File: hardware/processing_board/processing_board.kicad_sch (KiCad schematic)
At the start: 43 parts, among them J1 USB_C_Receptacle_USB2.0_14P, J2 USB_C_Receptacle_USB2.0_14P, J3 S2B-PH-K-S_LF__SN_, U1 BQ24075RGT, U2 NCP1117-3.3_SOT223, U3 TPS62821DLC, U4 TPS22917DBV, U5 NCP1117-1.8_SOT223

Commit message: Added FPGA bypass caps
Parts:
- added C15: 3.3uF, symbol Device:C_Small_US
- added C16, C17: 18pF, symbol Device:C_Small_US
- added C18, C19, C20, C21, C22, C23, C24, C25, C26, C28: 0.1uF, symbol Device:C_Small_US
- added C27: 4.7uF, symbol Device:C_Small_US
- added C29: 100nF, symbol Device:C_Small_US
- added FB1: 600@100MHZ, symbol Device:FerriteBead_Small
- added IC1: XC7S25-2CSGA225I, BGA225C80P15X15_1300X1300X140, symbol XC7S25-2CSGA225I:XC7S25-2CSGA225I
- added J4: Micro_SD_Card_Det1, symbol Connector:Micro_SD_Card_Det1
- added R14: 12k, symbol Device:R_Small
- added R15, R24: 10k, symbol Device:R_Small
- added R16, R17: 1k, symbol Device:R_Small
- added R21: 2.2k, symbol Device:R_Small
- added R22: 330, symbol Device:R_Small
- added R23: 4.7k, symbol Device:R_Small
- added SW1: SW_Push, symbol Switch:SW_Push
- added TP4: GND_TP, TestPoint:TestPoint_Loop_D2.60mm_Drill0.9mm_Beaded, symbol Connector:TestPoint
- added U6: FT2232HQ, Package_DFN_QFN:QFN-64-1EP_9x9mm_P0.5mm_EP4.35x4.35mm, symbol Interface_USB:FT2232HQ
- added U7: 93LCxxA, symbol Memory_EEPROM:93LCxxA
- added U8: W25Q32JVSS, Package_SO:SOIC-8_5.3x5.3mm_P1.27mm, symbol Memory_Flash:W25Q32JVSS
- added X1: ESP32-S3-WROOM-1-N16R8, ESP32-S3-WROOM-1-N16R8:ESP32S3WROOM1N8R2, symbol ESP32-S3-WROOM-1-N16R8:ESP32-S3-WROOM-1-N16R8
- added Y1: Crystal, symbol Device:Crystal
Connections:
- net +1V0: now also IC1.E10 (VCCINT_2), IC1.E8 (VCCINT_1), IC1.F7 (VCCINT_3), IC1.G10 (VCCINT_4), IC1.G6 (VCCBRAM_1), IC1.H7 (VCCINT_5), IC1.J10 (VCCINT_6), IC1.J6 (VCCBRAM_2), IC1.K7 (VCCINT_7), IC1.K9 (VCCINT_8)
- net +1V8: now also FB1.1
- net +3V3: now also C18.1, C28.1, C29.1, IC1.B7 (VCCO_15_1), IC1.C11 (VCCO_15_2), IC1.C3 (VCCO_34_1), IC1.E6 (VCCO_0_1), IC1.G2 (VCCO_34_2), IC1.H5 (CFGBVS_0), IC1.J14 (VCCO_14_1), J4.4 (VDD), R15.1, R16.1, R22.1, R23.2, R24.1, U6.19 (ADBUS3), U6.50 (VREGIN), U7.8 (VCC), U8.8 (VCC), X1.2 (3V3)
- net FPGA_D+: now also U6.8 (DP)
- net FPGA_D-: now also U6.7 (DM)
- net GND: now also C15.2, C16.2, C17.2, C18.2, C19.2, C20.2, C21.2, C22.2, C23.2, C24.2, C25.2, C26.2, C27.2, C28.2, C29.2, IC1.A1 (GND_1), IC1.A15 (GND_2), IC1.B8 (GND_3), IC1.C12 (GND_5), IC1.C2 (GND_4), IC1.D14 (GND_7), IC1.D5 (VCCBATT_0), IC1.D6 (GND_6), IC1.E4 (GND_8), IC1.E7 (GND_9), IC1.E9 (GND_10), IC1.F10 (GND_12), IC1.F13 (GND_13), IC1.F6 (GND_11), IC1.F8 (GNDADC_0), IC1.G3 (GND_14), IC1.G8 (VREFN_0), IC1.G9 (VP_0), IC1.H10 (GND_17), IC1.H6 (GND_16), IC1.H8 (VN_0), IC1.H9 (VREFP_0), IC1.J13 (GND_19), IC1.J7 (GND_18), IC1.K10 (GND_22), IC1.K6 (GND_20), IC1.K8 (GND_21), IC1.L2 (GND_23), IC1.L7 (GND_24), IC1.L9 (GND_25), IC1.M11 (GND_26), IC1.P13 (GND_29), IC1.P4 (GND_27), IC1.P8 (GND_28), IC1.R1 (GND_30), IC1.R15 (GND_31), J4.10 (SHIELD), J4.6 (VSS), R14.1, R17.2, SW1.2, TP4.1, U6.1 (GND), U6.10 (AGND), U6.11 (GND), U6.15 (GND), U6.25 (GND), U6.35 (GND), U6.47 (GND), U6.5 (GND), U6.51 (GND), U6.65 (GND), U7.5 (GND), U8.4 (GND), X1.1 (GND), X1.40 (GND), X1.41 (GND), X1.42 (GND), X1.43 (GND), X1.44 (GND), X1.45 (GND), X1.46 (GND), X1.47 (GND), X1.48 (GND), X1.49 (GND)
- new net: C16.1, C17.1, U6.3 (OSCO), Y1.1
- new net: R15.2, U6.14 (~{RESET})
- new net: R21.1, U7.3 (DI)
- new net: R21.2, U6.61 (EEDATA), U7.4 (DO)
- new net: C26.1, C27.1, FB1.2, IC1.F9 (VCCADC_0)
- new net: IC1.G5 (DONE_0), R22.2
- new net: U6.2 (OSCI), Y1.2
- new net: R14.2, U6.6 (REF)
- new net: IC1.J5 (PROGRAM_B_0), R23.1, SW1.1
- new net BOOT: X1.27 (IO0)
- new net D+: X1.14 (IO20)
- new net D-: X1.13 (IO19)
- new net EECLK: U6.62 (EECLK), U7.2 (SCLK)
- new net EECS: U6.63 (EECS), U7.1 (CS)
- new net EN: X1.3 (EN)
- new net FLASH_CLK: IC1.F5 (CCLK_0), U8.6 (CLK)
- new net FLASH_CS: U8.1 (~{CS})
- new net FLASH_DI: IC1.H14 (IO_L1P_T0_D00_MOSI_14), U8.2 (DO/IO_{1})
- new net FLASH_DO: IC1.H15 (IO_L1N_T0_D01_DIN_14), U8.5 (DI/IO_{0})
- new net FLASH_HOLD: U8.7 (~{HOLD}/~{RESET}/IO_{3})
- new net FLASH_WP: IC1.J12 (IO_L2P_T0_D02_14), U8.3 (~{WP}/IO_{2})
- new net INT: X1.38 (IO2)
- new net IO11: X1.19 (IO11)
- new net IO12: X1.20 (IO12)
- new net IO13: X1.21 (IO13)
- new net IO14: X1.22 (IO14)
- new net IO4: X1.4 (IO4)
- new net IO5: X1.5 (IO5)
- new net IO6: X1.6 (IO6)
- new net IO7: X1.7 (IO7)
- new net IO8: X1.12 (IO8)
- new net RX: IC1.B5 (IO_L5N_T0_34)
- new net SD_CLK: J4.5 (CLK)
- new net SD_CMD: J4.3 (CMD)
- new net SD_DAT0: J4.7 (DAT0)
- new net SD_DAT3: J4.2 (DAT3/CD)
- new net SD_DET: J4.9 (DET), R24.2
- new net TCK: IC1.E5 (TCK_0), R17.1, U6.16 (ADBUS0)
- new net TDI: U6.17 (ADBUS1)
- new net TDO: IC1.K4 (TDO_0), U6.18 (ADBUS2)
- new net TMS: IC1.K5 (TMS_0), R16.2
- new net TX: IC1.C5 (IO_L5P_T0_34)
- new net VCCIO: C22.1, C23.1, C24.1, C25.1, U6.20 (VCCIO), U6.31 (VCCIO), U6.42 (VCCIO), U6.56 (VCCIO)
- new net VCORE: C19.1, C20.1, C21.1, U6.12 (VCORE), U6.37 (VCORE), U6.64 (VCORE)
- new net VPHY: U6.4 (VPHY)
- new net VPLL: U6.9 (VPLL)
- new net VREGOUT: C15.1, U6.49 (VREGOUT)
- no-connect marks 3 -> 58
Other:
- note added: "ESP32"
- moved on the sheet: C11, C12, C13, C14, C8, C9, R11, U4, U5

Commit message: Schematic is a disaster, passes ERC
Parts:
- removed J4: Micro_SD_Card_Det1, symbol Connector:Micro_SD_Card_Det1
- removed TP4: GND_TP, TestPoint:TestPoint_Loop_D2.60mm_Drill0.9mm_Beaded, symbol Connector:TestPoint
- removed U5: NCP1117-1.8_SOT223, Package_TO_SOT_SMD:SOT-223-3_TabPin2, symbol Regulator_Linear:NCP1117-1.8_SOT223
- added C30: 0.1uF, Capacitor_SMD:C_0805_2012Metric, symbol Device:C_Small_US
- added C31, C77, C78, C80: 0.1uF, symbol Device:C_Small_US
- added C32, C33, C41, C42, C47, C48, C55, C56, C60, C61, C71, C72, C73: 47nF, symbol Device:C_Small_US
- added C34, C35, C36, C37, C43, C44, C45, C46, C49, C50, C51, C52, C57, C62, C63, C66, C67, C74, C75: 470nF, symbol Device:C_Small_US
- added C38, C39, C53, C54, C59, C64, C68, C69: 4.7uF, symbol Device:C_Small_US
- added C40, C70: 100uF, symbol Device:C_Small_US
- added C58, C65: 47uF, symbol Device:C_Small_US
- added C76: 10nF, symbol Device:C_Small_US
- added C79, C81, C82: 0.01uF, symbol Device:C_Small_US
- added FB2: 600@100MHZ, symbol Device:FerriteBead_Small
- added FB3, FB4: 600@100MHz, symbol Device:FerriteBead_Small
- added J4: Conn_02x07_Counter_Clockwise, symbol Connector_Generic:Conn_02x07_Counter_Clockwise
- added LS1: Speaker, symbol Device:Speaker
- added R25, R26: 10k, Resistor_SMD:R_0805_2012Metric, symbol Device:R_Small
- added R27, R32: 4.7k, symbol Device:R_Small
- added R28, R29, R30, R31: 1k, symbol Device:R_Small
- added R33, R34, R35, R42: 10k, symbol Device:R_Small
- added R36, R37, R38, R39: 100, symbol Device:R_Small
- added R40, R41: 50, symbol Device:R_Small
- added SW2: BOOT_BTN, Button_Switch_SMD:SW_SPST_B3U-1000P, symbol Switch:SW_Push
- added SW3: RST_BTN, Button_Switch_SMD:SW_SPST_B3U-1000P, symbol Switch:SW_Push
- added U10: MAX98357A, Package_DFN_QFN:TQFN-16-1EP_3x3mm_P0.5mm_EP1.23x1.23mm, symbol Audio:MAX98357A
- added U11: LP2985-1.8, Package_TO_SOT_SMD:SOT-23-5, symbol Regulator_Linear:LP2985-1.8
- added U9: W25Q128JVS, Package_SO:SOIC-8_5.3x5.3mm_P1.27mm, symbol Memory_Flash:W25Q128JVS
- added Y2: ECS-2520MV-xxx-xx, Oscillator:Oscillator_SMD_ECS_2520MV-xxx-xx-4Pin_2.5x2.0mm, symbol Oscillator:ECS-2520MV-xxx-xx
- C2: value 10uF -> 22uF
- C26: value 0.1uF -> 47nF
- C27: value 4.7uF -> 470nF
- C29: value 100nF -> 0.1uF
- R22: value 330 -> 200
- R24: value 10k -> 100k
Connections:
- net 3V3_FPGA is gone; now on net +3.3V: C9.1, R13.1, U4.5 (QOD), U4.6 (VOUT)
- net D+ is gone; now on net ESP_D+: X1.14 (IO20)
- net D- is gone; now on net ESP_D-: X1.13 (IO19)
- net RX is gone; now on net ESP_TX: IC1.B5 (IO_L5N_T0_34)
- net TMS is gone; now on net +3.3V: IC1.K5 (TMS_0), R16.2
- net TX is gone; now on net ESP_RX: IC1.C5 (IO_L5P_T0_34)
- net +1V0: now also C55.1, C56.1, C57.1, C58.1, C59.1, C66.1, C67.1, C68.1, C69.1, C70.1, C71.1, C72.1, C73.1, C74.1
- net +1V8: now also IC1.D5 (VCCBATT_0), IC1.L6 (VCCAUX_1), IC1.L8 (VCCAUX_2), C60.1, C61.1, C62.1, C63.1, C64.1, C65.1, U11.5 (VOUT)
- net +3V3: now also C30.1, C77.1, R25.2, R26.2, R33.2, R34.2, R35.2, R42.1, U10.7 (VDD), U10.8 (VDD), U11.1 (VIN), U9.8 (VCC); no longer C28.1, IC1.B7 (VCCO_15_1), IC1.C11 (VCCO_15_2), IC1.C3 (VCCO_34_1), IC1.E6 (VCCO_0_1), IC1.G2 (VCCO_34_2), IC1.H5 (CFGBVS_0), IC1.J14 (VCCO_14_1), R16.1, R22.1, R23.2, U6.19 (ADBUS3), U8.8 (VCC)
- net 1V0_PG: now also R42.2, U11.3 (ON/~{OFF})
- net BOOT: now also R26.1, SW2.2
- net EN: now also R25.1, SW3.2
- net FLASH_CLK: now also R40.1; no longer IC1.F5 (CCLK_0)
- net FLASH_CS: now also IC1.L11 (IO_L6P_T0_FCS_B_14)
- net FLASH_DI: now also R36.2; no longer IC1.H14 (IO_L1P_T0_D00_MOSI_14)
- net FLASH_DO: now also R37.2; no longer IC1.H15 (IO_L1N_T0_D01_DIN_14)
- net FLASH_HOLD: now also R39.2
- net FLASH_WP: now also R38.2; no longer IC1.J12 (IO_L2P_T0_D02_14)
- net GND: now also IC1.G7 (GND_15), C30.2, C31.2, C32.2, C33.2, C34.2, C35.2, C36.2, C37.2, C38.2, C39.2, C40.2, C41.2, C42.2, C43.2, C44.2, C45.2, C46.2, C47.2, C48.2, C49.2, C50.2, C51.2, C52.2, C53.2, C54.2, C55.2, C56.2, C57.2, C58.2, C59.2, C60.2, C61.2, C62.2, C63.2, C64.2, C65.2, C66.2, C67.2, C68.2, C69.2, C70.2, C71.2, C72.2, C73.2, C74.2, C75.2, C77.2, C78.2, C79.2, C80.2, C81.2, C82.2, FB2.2, J4.8 (Pin_8), R30.2, R31.2, SW2.1, SW3.1, U10.11 (GND), U10.15 (GND), U10.17 (PAD), U10.3 (GND), U11.2 (GND), U9.4 (GND), Y2.2 (GND); no longer IC1.D5 (VCCBATT_0), IC1.F8 (GNDADC_0)
- net TDI: now also IC1.L4 (TDI_0)
- net VPHY: now also C78.1, C79.1, FB3.1
- net VPLL: now also C80.1, C81.1, FB4.1
- net ESP_TX: now reaches X1.17 (IO9)
- net ESP_CS: now reaches X1.18 (IO10)
- net ESP_CS: now also R35.1, U9.1 (~{CS})
- net +3.3V: now reaches C26.1, C27.1
- net +3.3V: now also C28.1, IC1.B7 (VCCO_15_1), IC1.C11 (VCCO_15_2), IC1.C3 (VCCO_34_1), IC1.E6 (VCCO_0_1), IC1.F12 (VCCO_15_3), IC1.G2 (VCCO_34_2), IC1.J14 (VCCO_14_1), IC1.L3 (VCCO_34_3), IC1.M12 (VCCO_14_2), IC1.P5 (VCCO_0_2), IC1.P9 (VCCO_14_3), R22.1, R23.2, U8.8 (VCC), C31.1, C32.1, C33.1, C34.1, C35.1, C36.1, C37.1, C38.1, C39.1, C40.1, C41.1, C42.1, C43.1, C44.1, C45.1, C46.1, C47.1, C48.1, C49.1, C50.1, C51.1, C52.1, C53.1, C54.1, FB3.2, FB4.2, J4.7 (Pin_7), R27.1, R28.1, R29.1, R32.1, Y2.1 (Tri-State), Y2.4 (VDD); no longer FB1.2, IC1.F9 (VCCADC_0)
- net BRIDGE_TX: now reaches U6.38 (BDBUS0)
- net BRIDGE_TX: now also IC1.K15 (IO_L5N_T0_D07_14)
- net BRIDGE_RX: now reaches U6.39 (BDBUS1)
- net BRIDGE_RX: now also IC1.L12 (IO_L6N_T0_D08_VREF_14)
- net FPGA_IO2: now reaches IC1.A3 (IO_L1N_T0_34)
- net FPGA_IO2: now also J4.2 (Pin_2)
- net FPGA_IO1: now reaches IC1.A4 (IO_L1P_T0_34)
- net FPGA_IO1: now also J4.1 (Pin_1)
- net FPGA_IO9: now reaches IC1.A5 (IO_L5P_T0_AD2P_15)
- net FPGA_IO9: now also J4.11 (Pin_11)
- net FPGA_IO10: now reaches IC1.A6 (IO_L5N_T0_AD2N_15)
- net FPGA_IO10: now also J4.12 (Pin_12)
- net FPGA_IO11: now reaches IC1.A8 (IO_L6P_T0_15)
- net FPGA_IO11: now also J4.13 (Pin_13)
- net FPGA_IO12: now reaches IC1.A9 (IO_L6N_T0_VREF_15)
- net FPGA_IO12: now also J4.14 (Pin_14)
- net FPGA_IO4: now reaches IC1.B3 (IO_L3N_T0_DQS_34)
- net FPGA_IO4: now also J4.4 (Pin_4)
- net FPGA_IO3: now reaches IC1.B4 (IO_L3P_T0_DQS_34)
- net FPGA_IO3: now also J4.3 (Pin_3)
- net FPGA_IO7: now reaches IC1.C6 (IO_L1P_T0_AD0P_15)
- net FPGA_IO7: now also J4.9 (Pin_9)
- net FPGA_IO8: now reaches IC1.C7 (IO_L1N_T0_AD0N_15)
- net FPGA_IO8: now also J4.10 (Pin_10)
- net FPGA_IO6: now reaches IC1.D1 (IO_L6N_T0_VREF_34)
- net FPGA_IO6: now also J4.6 (Pin_6)
- net FPGA_IO5: now reaches IC1.D2 (IO_L6P_T0_34)
- net FPGA_IO5: now also J4.5 (Pin_5)
- net at IC1.K11 (IO_L3P_T0_DQS_PUDC_B_14): now also R28.2
- net at IC1.K13 (IO_L2N_T0_D03_14): now also R39.1
- net at IC1.L5 (INIT_B_0): now also R27.2
- net at IC1.M5 (M0_0): now also R29.2
- net at IC1.M6 (M2_0): now also R30.1
- net at IC1.M9 (IO_L13P_T2_MRCC_14): now also R41.1
- net at IC1.N5 (M1_0): now also R31.1
- net INT: no longer names the net of X1.38 (IO2)
- net IO11 renamed ESP_DI
- net ESP_DI: now also U9.5 (DI/IO_{0})
- net IO12 renamed ESP_CLK
- net ESP_CLK: now also U9.6 (CLK)
- net IO13 renamed ESP_DO
- net ESP_DO: now also U9.2 (DO/IO_{1})
- net IO14: no longer names the net of X1.22 (IO14)
- net IO4 renamed MAX_DIN
- net MAX_DIN: now also U10.1 (DIN)
- net IO5 renamed MAX_BCLK
- net MAX_BCLK: now also U10.16 (BCLK)
- net IO6 renamed MAX_LRCLK
- net MAX_LRCLK: now also U10.14 (LRCLK)
- net IO7 renamed MAX_SDMODE
- net MAX_SDMODE: now also U10.4 (~{SD_MODE})
- net IO8 renamed ESP_RX
- net SD_DET: no longer names the net of R24.2
- net SD_DET: now also U10.2 (GAIN_SLOT)
- new net: IC1.H14 (IO_L1P_T0_D00_MOSI_14), R36.1
- new net: LS1.2, U10.10 (OUTN)
- new net: LS1.1, U10.9 (OUTP)
- new net: R41.2, Y2.3 (OUT)
- new net: R34.1, U9.3 (~{WP}/IO_{2})
- new net: R33.1, U9.7 (~{HOLD}/~{RESET}/IO_{3})
- new net: IC1.J12 (IO_L2P_T0_D02_14), R38.1
- new net: R16.1, U6.19 (ADBUS3)
- new net: C82.1, U11.4 (BP)
- new net: IC1.H5 (CFGBVS_0), R32.2
- new net: IC1.H15 (IO_L1N_T0_D01_DIN_14), R37.1
- new net: IC1.F5 (CCLK_0), R40.2
- new net GNDADC_0: C76.2, FB2.1, IC1.F8 (GNDADC_0)
- new net VCCADC_0: C75.1, C76.1, FB1.2, IC1.F9 (VCCADC_0)
- no-connect marks 58 -> 184
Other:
- note added: "AUDIO DRIVER"
- note added: "ESP BUTTONS"
- note added: "ESP32 FLASH"
- note added: "FPGA FLASH"
- note added: "USB-C TO JTAG BRIDGE"
- moved on the sheet: C11, C12, C13, C14, C15, C16, C17, C18, C19, C20, C21, C22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

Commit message: Added all footprints
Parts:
- C1, C11, C12, C16, C17, C18, C19, C20, C21, C22, C23, C24, C25, C26, C27, C28, C29, C31, C32, C33, C34, C35, C36, C37, C41, C42, C43, C44, C45, C46, C47, C48, C49, C50, C51, C52, C55, C56, C57, C6, C60, C61, C62, C63, C66, C67, C71, C72, C73, C74, C75, C76, C77, C78, C79, C8, C80, C81, C82, C9: footprint (none) -> Capacitor_SMD:C_0402_1005Metric
- C13, C14, C2, C4, C40, C5, C58, C65, C7, C70: footprint (none) -> Capacitor_SMD:C_0805_2012Metric
- C15, C38, C39, C53, C54, C59, C64, C68, C69, FB1, FB2, FB3, FB4: footprint (none) -> Capacitor_SMD:C_0603_1608Metric
- C3: footprint Capacitor_SMD:C_0805_2012Metric -> Capacitor_SMD:C_0603_1608Metric
- C30: footprint Capacitor_SMD:C_0805_2012Metric -> Capacitor_SMD:C_0402_1005Metric
- D1, D3, D4: footprint (none) -> LED_SMD:LED_0805_2012Metric
- IC1: footprint BGA225C80P15X15_1300X1300X140 -> SPAR_FPGA:BGA225C80P15X15_1300X1300X140
- J1, J2: footprint (none) -> Connector_USB:USB_C_Receptacle_JAE_DX07S016JA1R1500
- J4: footprint (none) -> Connector_PinHeader_2.54mm:PinHeader_2x07_P2.54mm_Vertical
- L1: footprint (none) -> DFE201612E-R47M_P2:INDC2016X120N
- LS1: footprint (none) -> Connector_JST:JST_PH_S2B-PH-K_1x02_P2.00mm_Horizontal
- R1, R10, R11, R12, R13, R14, R15, R16, R17, R2, R21, R22, R23, R24, R27, R28, R29, R3, R30, R31, R32, R33, R34, R35, R36, R37, R38, R39, R4, R40, R41, R42, R5, R8, R9: footprint (none) -> Resistor_SMD:R_0402_1005Metric
- R18, R19, R20, R25, R26: footprint Resistor_SMD:R_0805_2012Metric -> Resistor_SMD:R_0402_1005Metric
- SW1: footprint (none) -> Button_Switch_SMD:SW_SPST_B3U-1000P
- U7: footprint (none) -> Oscillator:Oscillator_SMD_ECS_2520MV-xxx-xx-4Pin_2.5x2.0mm
- Y1: footprint (none) -> Crystal:Crystal_SMD_3225-4Pin_3.2x2.5mm

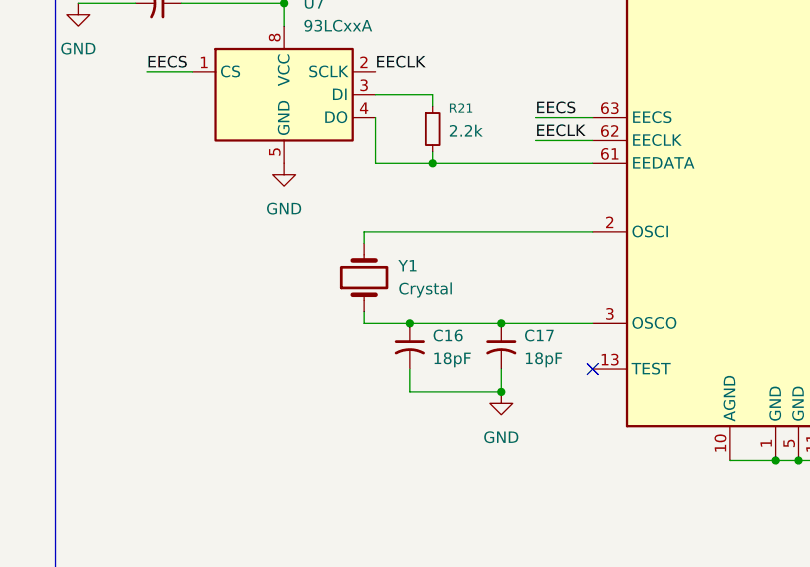
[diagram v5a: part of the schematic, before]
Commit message: Created netlist and imported it to the PCB editor
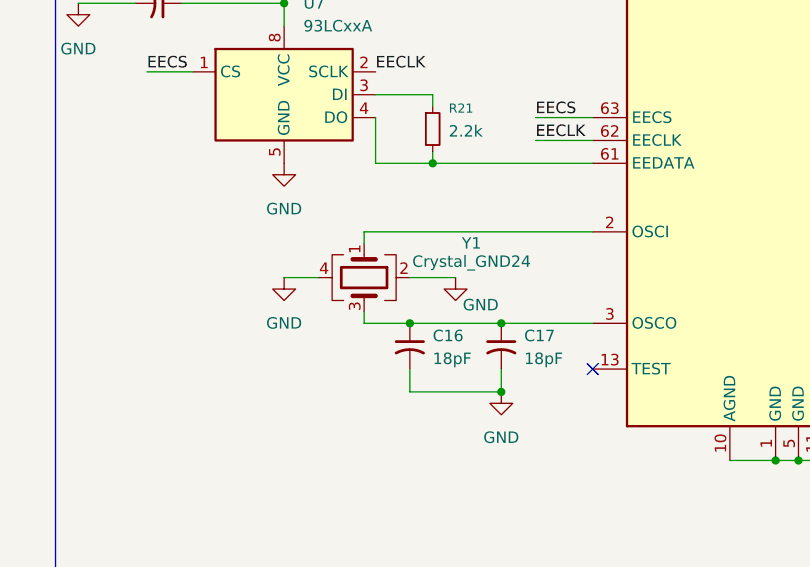
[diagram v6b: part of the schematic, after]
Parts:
- removed Y1: Crystal, Crystal:Crystal_SMD_3225-4Pin_3.2x2.5mm, symbol Device:Crystal
- added Y1: Crystal_GND24, Crystal:Crystal_SMD_3225-4Pin_3.2x2.5mm, symbol Device:Crystal_GND24
- U7: footprint Oscillator:Oscillator_SMD_ECS_2520MV-xxx-xx-4Pin_2.5x2.0mm -> Package_SO:SOIC-8_3.9x4.9mm_P1.27mm
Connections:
- net GND: now also Y1.2, Y1.4
- net at C16.1, C17.1, U6.3 (OSCO): now also Y1.3
- net at U6.2 (OSCI): now also Y1.1
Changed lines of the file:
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@@
 	(wire
 		(pts
+			(xy 237.49 195.58) (xy 232.41 195.58)
+		)
+		(stroke
+			(width 0)
+			(type default)
+		)
+	)
+	(wire
+		(pts
 			(xy 322.58 44.45) (xy 331.47 44.45)
 		)
@@
 	(wire
 		(pts
+			(xy 218.44 195.58) (xy 222.25 195.58)
+		)
+		(stroke
+			(width 0)
+			(type default)
+		)
+	)
+	(wire
+		(pts
 			(xy 350.52 191.77) (xy 350.52 189.23)
 		)
@@
 	)
 	(symbol
+		(lib_id "Device:Crystal_GND24")
+		(at 227.33 195.58 270)
+		(unit 1)
+		(exclude_from_sim no)
+		(in_bom yes)
+		(on_board yes)
+		(dnp no)
+		(property "Reference" "Y1"
+			(at 239.268 191.77 90)
+			(effects
+				(font
+					(size 1.27 1.27)
+				)
+			)
+		)
+		(property "Value" "Crystal_GND24"
+			(at 239.268 193.802 90)
+			(effects
+				(font
+					(size 1.27 1.27)
+				)
+			)
+		)
+		(property "Footprint" "Crystal:Crystal_SMD_3225-4Pin_3.2x2.5mm"
+			(at 227.33 195.58 0)
+			(effects
+				(font
+					(size 1.27 1.27)
+				)
+				(hide yes)
+			)
+		)
+		(property "Datasheet" "~"
+			(at 227.33 195.58 0)
+			(effects
+				(font
+					(size 1.27 1.27)
+				)
+				(hide yes)
+			)
+		)
+		(property "Description" "Four pin crystal, GND on pins 2 and 4"
+			(at 227.33 195.58 0)
+			(effects
+				(font
+					(size 1.27 1.27)
+				)
+				(hide yes)
+			)
+		)
+		(pin "2"
+		)
+		(pin "1"
+		)
+		(pin "3"
+		)
+		(pin "4"
+		)
+		(instances
+			(project ""
+				(path "/de118238-5cf0-4f20-b51d-7acba9897a1d"
+					(reference "Y1")
+					(unit 1)
+				)
+			)
+		)
+	)
+	(symbol
 		(lib_id "Device:R_Small")
 		(at 82.55 120.65 0)
@@
 	)
 	(symbol
+		(lib_id "power:GND")
+		(at 237.49 195.58 0)
+		(unit 1)
+		(exclude_from_sim no)
+		(in_bom yes)
+		(on_board yes)
+		(dnp no)
+		(property "Reference" "#PWR0142"
+			(at 237.49 201.93 0)
+			(effects
+				(font
+					(size 1.27 1.27)
+				)
+				(hide yes)
+			)
+		)
+		(property "Value" "GND"
+			(at 240.284 198.628 0)
+			(effects
+				(font
+					(size 1.27 1.27)
+				)
+			)
+		)
+		(property "Footprint" ""
+			(at 237.49 195.58 0)
+			(effects
+				(font
+					(size 1.27 1.27)
+				)
+				(hide yes)
+			)
+		)
+		(property "Datasheet" ""
+			(at 237.49 195.58 0)
+			(effects
+				(font
+					(size 1.27 1.27)
+				)
+				(hide yes)
+			)
+		)
+		(property "Description" "Power symbol creates a global label with name \"GND\" , ground"
+			(at 237.49 195.58 0)
+			(effects
+				(font
+					(size 1.27 1.27)
+				)
+				(hide yes)
+			)
+		)
+		(pin "1"
+		)
+		(instances
+			(project ""
+				(path "/de118238-5cf0-4f20-b51d-7acba9897a1d"
+					(reference "#PWR0142")
+					(unit 1)
+				)
+			)
+		)
+	)
+	(symbol
 		(lib_id "power:+3.3V")
 		(at 506.73 172.72 0)
@@
 	(symbol
 		(lib_id "power:GND")
+		(at 218.44 195.58 0)
+		(unit 1)
+		(exclude_from_sim no)
+		(in_bom yes)
+		(on_board yes)
+		(dnp no)
+		(fields_autoplaced yes)
+		(property "Reference" "#PWR0143"
+			(at 218.44 201.93 0)
+			(effects
+				(font
+					(size 1.27 1.27)
+				)
+				(hide yes)
+			)
+		)
+		(property "Value" "GND"
+			(at 218.44 200.66 0)
+			(effects
+				(font
+					(size 1.27 1.27)
+				)
+			)
+		)
+		(property "Footprint" ""
+			(at 218.44 195.58 0)
+			(effects
+				(font
+					(size 1.27 1.27)
+				)
+				(hide yes)
+			)
+		)
+		(property "Datasheet" ""
+			(at 218.44 195.58 0)
+			(effects
+				(font
+					(size 1.27 1.27)
+				)
+				(hide yes)
+			)
+		)
+		(property "Description" "Power symbol creates a global label with name \"GND\" , ground"
+			(at 218.44 195.58 0)
+			(effects
+				(font
+					(size 1.27 1.27)
+				)
+				(hide yes)
+			)
+		)
+		(pin "1"
+		)
+		(instances
+			(project ""
+				(path "/de118238-5cf0-4f20-b51d-7acba9897a1d"
+					(reference "#PWR0143")
+					(unit 1)
+				)
+			)
+		)
+	)
+	(symbol
+		(lib_id "power:GND")
 		(at 30.48 267.97 0)
 		(unit 1)
@@
 			)
 		)
-		(property "Footprint" "Oscillator:Oscillator_SMD_ECS_2520MV-xxx-xx-4Pin_2.5x2.0mm"
+		(property "Footprint" "Package_SO:SOIC-8_3.9x4.9mm_P1.27mm"
 			(at 218.44 175.26 0)
 			(effects
@@
 					(unit 1)
 				)
-			)
-		)
-	)
-	(symbol
-		(lib_id "Device:Crystal")
-		(at 227.33 195.58 90)
-		(unit 1)
-		(exclude_from_sim no)
-		(in_bom yes)
-		(on_board yes)
-		(dnp no)
-		(fields_autoplaced yes)
-		(property "Reference" "Y1"
-			(at 231.14 194.3099 90)
-			(effects
-				(font
-					(size 1.27 1.27)
-				)
-				(justify right)
-			)
-		)
-		(property "Value" "Crystal"
-			(at 231.14 196.8499 90)
-			(effects
-				(font
-					(size 1.27 1.27)
-				)
-				(justify right)
-			)
-		)
-		(property "Footprint" "Crystal:Crystal_SMD_3225-4Pin_3.2x2.5mm"
-			(at 227.33 195.58 0)
-			(effects
-				(font
-					(size 1.27 1.27)
-				)
-				(hide yes)
-			)
-		)
-		(property "Datasheet" "~"
-			(at 227.33 195.58 0)
-			(effects
-				(font
-					(size 1.27 1.27)
-				)
-				(hide yes)
-			)
-		)
-		(property "Description" "Two pin crystal"
-			(at 227.33 195.58 0)
-			(effects
-				(font
-					(size 1.27 1.27)
-				)
-				(hide yes)
-			)
-		)
-		(pin "1"
-		)
-		(pin "2"
-		)
-		(instances
-			(project ""
-				(path "/de118238-5cf0-4f20-b51d-7acba9897a1d"
-					(reference "Y1")
-					(unit 1)
-				)

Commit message: Routed charging circuit
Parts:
- added TP1: 5V, TestPoint:TestPoint_Loop_D2.60mm_Drill0.9mm_Beaded, symbol Connector:TestPoint
- added TP10: CCLK_0, TestPoint:TestPoint_Loop_D2.60mm_Drill0.9mm_Beaded, symbol Connector:TestPoint
- added TP11: 12MHZ, TestPoint:TestPoint_Loop_D2.60mm_Drill0.9mm_Beaded, symbol Connector:TestPoint
- added TP12: Crystal, TestPoint:TestPoint_Loop_D2.60mm_Drill0.9mm_Beaded, symbol Connector:TestPoint
- added TP13: ESP_RX, TestPoint:TestPoint_Loop_D2.60mm_Drill0.9mm_Beaded, symbol Connector:TestPoint
- added TP14: ESP_TX, TestPoint:TestPoint_Loop_D2.60mm_Drill0.9mm_Beaded, symbol Connector:TestPoint
- added TP2: 3V3, TestPoint:TestPoint_Loop_D2.60mm_Drill0.9mm_Beaded, symbol Connector:TestPoint
- added TP3: 1V0, TestPoint:TestPoint_Loop_D2.60mm_Drill0.9mm_Beaded, symbol Connector:TestPoint
- added TP4: 1V8, TestPoint:TestPoint_Loop_D2.60mm_Drill0.9mm_Beaded, symbol Connector:TestPoint
- added TP5: 3.3V, TestPoint:TestPoint_Loop_D2.60mm_Drill0.9mm_Beaded, symbol Connector:TestPoint
- added TP6: GND, TestPoint:TestPoint_Loop_D2.60mm_Drill0.9mm_Beaded, symbol Connector:TestPoint
- added TP7: DONE_0, TestPoint:TestPoint_Loop_D2.60mm_Drill0.9mm_Beaded, symbol Connector:TestPoint
- added TP8: PROGRAM_B, TestPoint:TestPoint_Loop_D2.60mm_Drill0.9mm_Beaded, symbol Connector:TestPoint
- added TP9: INIT_B, TestPoint:TestPoint_Loop_D2.60mm_Drill0.9mm_Beaded, symbol Connector:TestPoint
- C10: footprint Capacitor_SMD:C_0805_2012Metric -> Resistor_SMD:R_0402_1005Metric
- R6, R7: footprint Resistor_SMD:R_0805_2012Metric -> Resistor_SMD:R_0402_1005Metric
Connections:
- net +1V0: now also TP3.1
- net +1V8: now also TP4.1
- net +3.3V: now also R15.1, U6.50 (VREGIN), TP5.1
- net +3V3: now also TP2.1; no longer R15.1, U6.50 (VREGIN)
- net +5V: now also TP1.1
- net ESP_RX: now also TP13.1
- net ESP_TX: now also TP14.1
- net GND: now also J3.1, TP6.1; no longer J3.2
- net at C10.1, C3.1, U1.2 (BAT)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: now also J3.2; no longer J3.1
- net at IC1.L5 (INIT_B_0), R27.2: now also TP9.1
- net at U6.2 (OSCI), Y1.1: now also TP12.1
- net at R41.2, Y2.3 (OUT): now also TP11.1
- net at IC1.G5 (DONE_0), R22.2: now also TP7.1
- net at IC1.J5 (PROGRAM_B_0), R23.1, SW1.1: now also TP8.1
- net at IC1.F5 (CCLK_0), R40.2: now also TP10.1
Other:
- moved on the sheet: J3, R22, R40
